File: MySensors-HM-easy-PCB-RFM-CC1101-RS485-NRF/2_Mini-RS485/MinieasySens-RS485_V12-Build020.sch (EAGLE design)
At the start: 38 parts, among them IC1 ATSHA204A, IC2 REG1117, IC4 REG1117, M1 ARDUINO-PRO-MINI-3.3V#NP, X1 1751264, X4 1751264

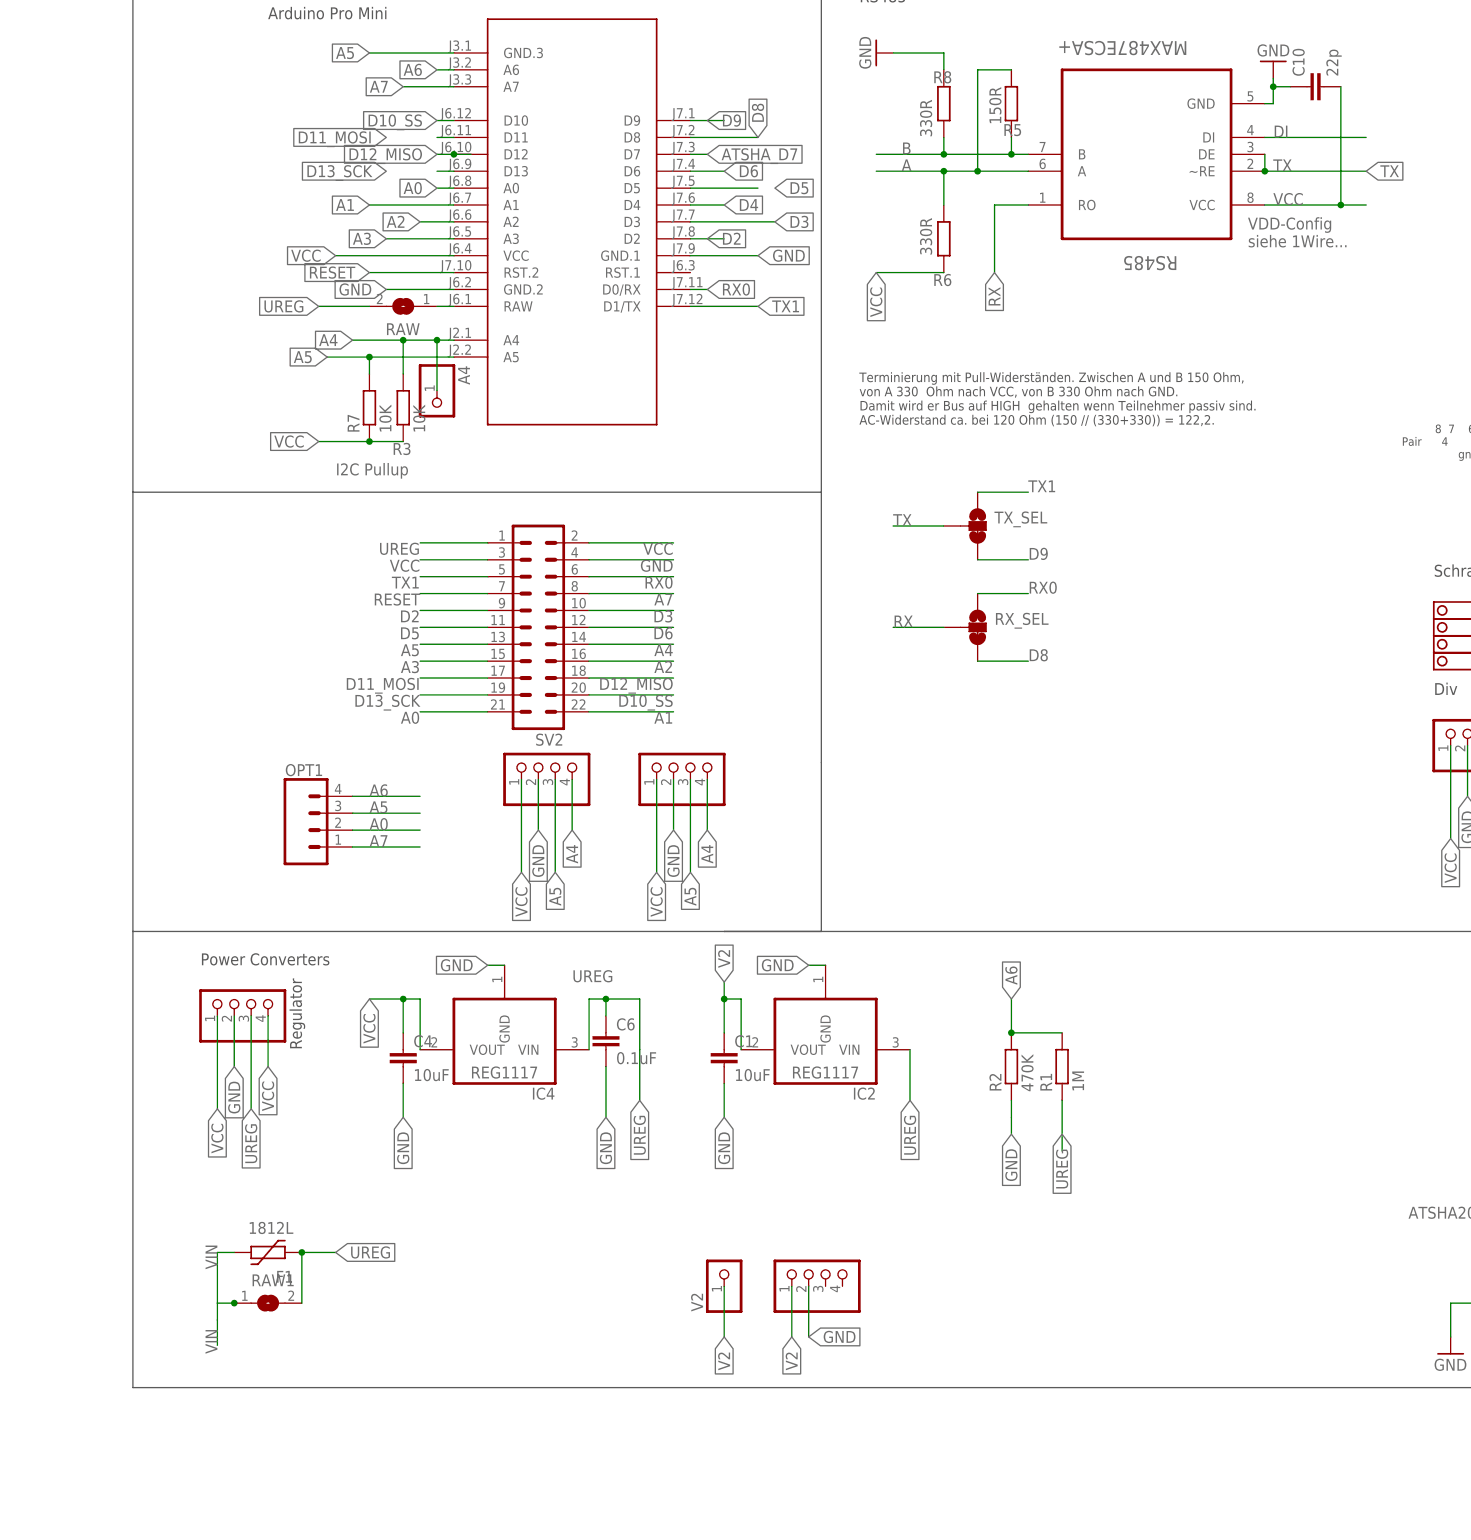
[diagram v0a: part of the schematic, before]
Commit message: BluePill, MiniRS485 Sensor+Gateway
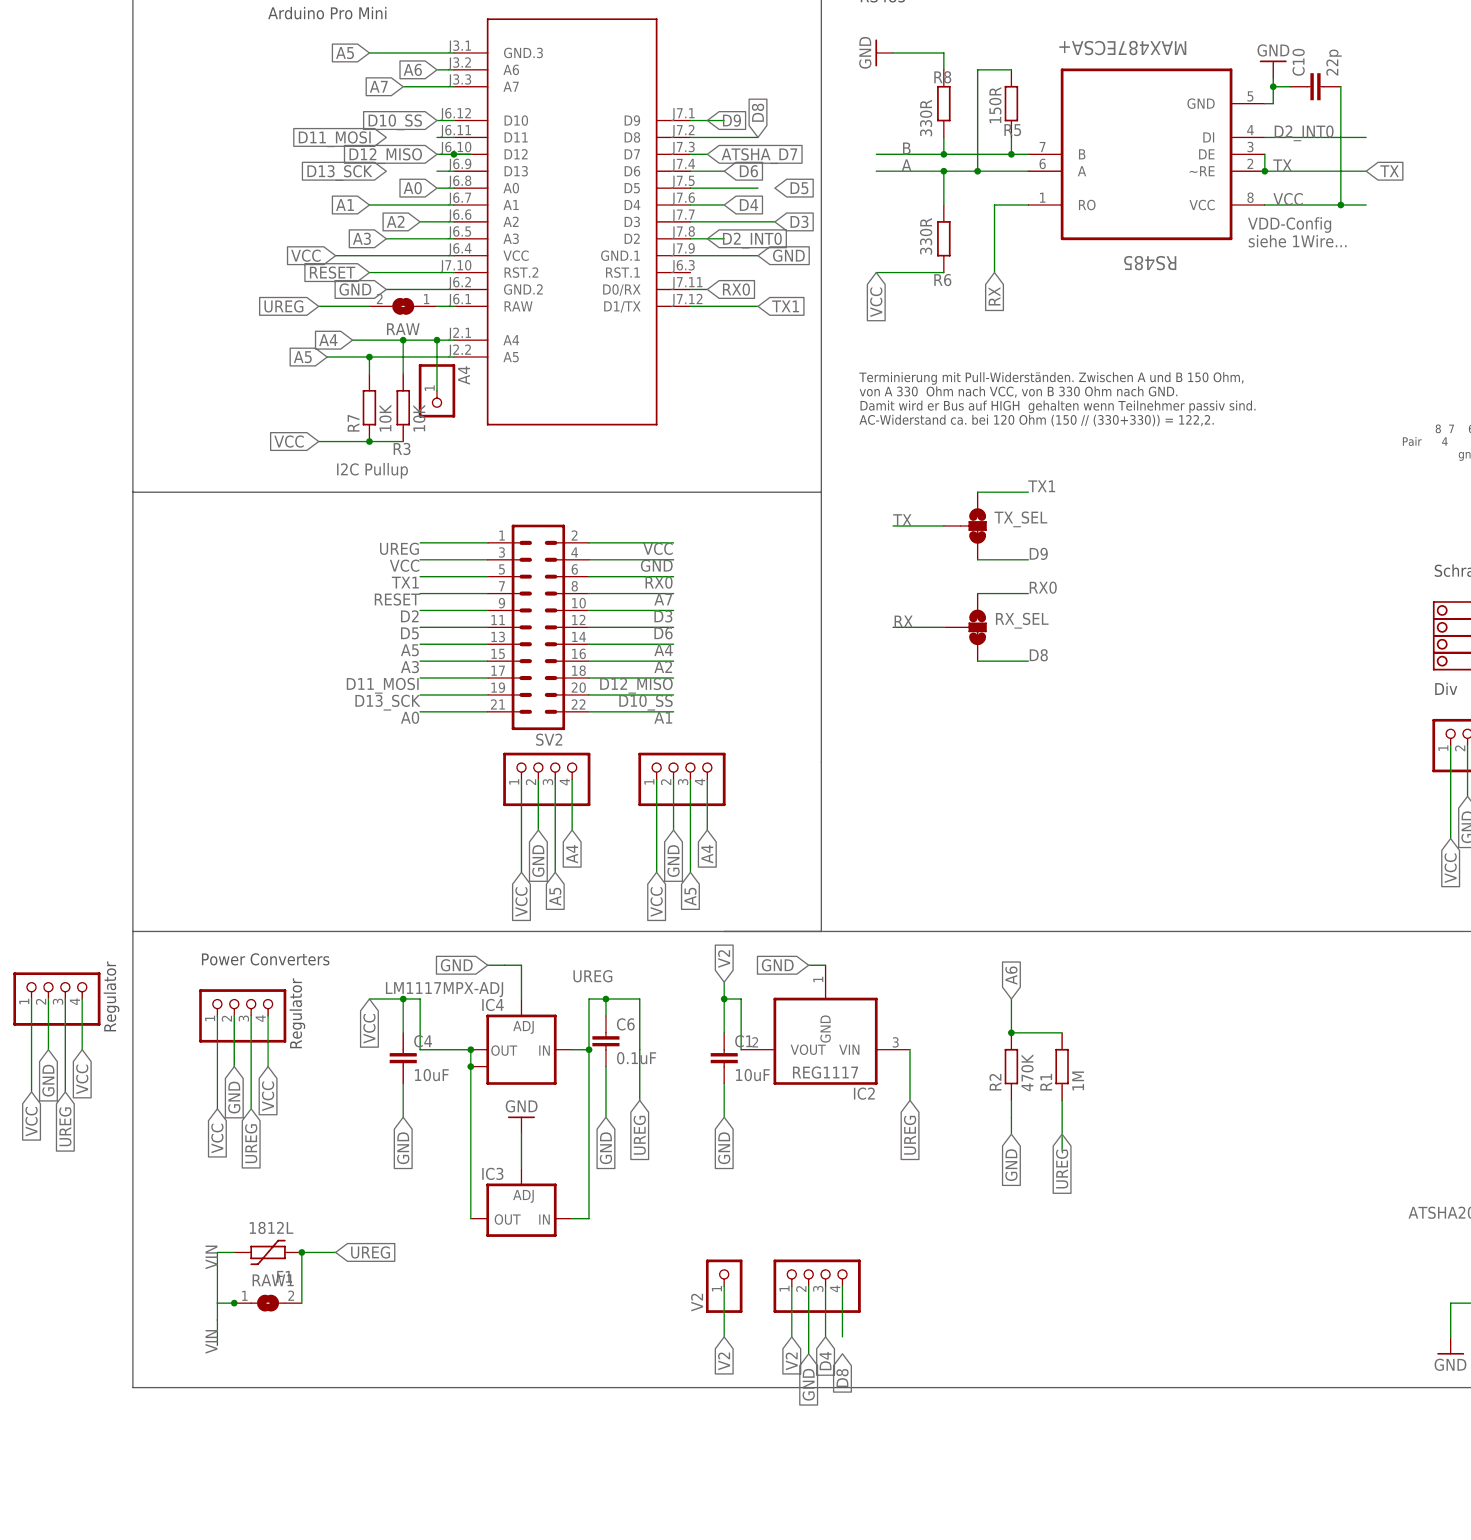
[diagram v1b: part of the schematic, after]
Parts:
- removed OPT1: (no value), SparkFun-Connectors:CONN_04
- added IC3: LD117ADT50TR, v-reg:LD117ADT50TR
- added STEPDWN1: (no value), pinhead-2:PINHD-1X04_2.54-S
- IC4: value REG1117 -> LM1117MPX-ADJ; device burr-brown:REG1117 -> lm1117:LM1117MPX-ADJ
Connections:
- removed net DI: RS485.DI
- new net D2_INT0: M1.D2, RS485.DI
- net A0: no longer OPT1.2
- net A5: no longer OPT1.3
- net A6: no longer OPT1.4
- net A7: no longer OPT1.1
- net D2: no longer M1.D2
- net D4: now also V2-.3
- net D8: now also V2-.4
- net GND: now also IC3.ADJ, IC4.ADJ, STEPDWN1.2; no longer IC4.GND
- net UREG: now also IC3.IN, IC4.IN, STEPDWN1.3; no longer IC4.VIN
- net VCC: now also IC3.OUT, IC4.OUT, IC4.OUT1, STEPDWN1.1, STEPDWN1.4; no longer IC4.VOUT
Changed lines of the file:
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@@
 <?xml version="1.0" encoding="utf-8"?>
 <!DOCTYPE eagle SYSTEM "eagle.dtd">
-<eagle version="7.6.0">
+<eagle version="7.7.0">
 <drawing>
 <settings>
@@
 <part name="C10" library="rcl" deviceset="C-EU" device="C0805" value="22p"/>
 <part name="R8" library="rcl" deviceset="R-EU_" device="R0805" value="330R"/>
-<part name="IC4" library="burr-brown" deviceset="REG1117" device=""/>
-<part name="OPT1" library="SparkFun-Connectors" deviceset="CONN_04" device=""/>
 <part name="STEPDWN" library="pinhead-2" deviceset="PINHD-1X04" device="_2.54-S"/>
 <part name="RAW1" library="jumper" deviceset="SJ" device=""/>
@@
 <part name="JP1" library="pinhead-2" deviceset="PINHD-1X04" device="_2.54-S"/>
 <part name="JP2" library="pinhead-2" deviceset="PINHD-1X04" device="_2.54-S"/>
+<part name="IC3" library="v-reg" deviceset="LD117A?*" device="DT" technology="50TR"/>
+<part name="GND1" library="supply1@1" deviceset="GND" device=""/>
+<part name="IC4" library="lm1117" deviceset="LM1117MPX-ADJ" device=""/>
+<part name="STEPDWN1" library="pinhead-2" deviceset="PINHD-1X04" device="_2.54-S"/>
 </parts>
 <sheets>
@@
 <wire x1="-2.54" y1="73.66" x2="12.065" y2="73.66" width="0.1524" layer="97"/>
 <wire x1="-2.54" y1="73.66" x2="161.925" y2="73.66" width="0.1524" layer="97"/>
+<text x="-93.98" y="58.42" size="1.778" layer="97" rot="R90">Regulator</text>
 </plain>
 <instances>
@@
 <attribute name="VALUE" x="28.702" y="193.04" size="1.778" layer="96" rot="R90"/>
 </instance>
-<instance part="IC4" gate="G$1" x="-35.56" y="55.88" rot="R180"/>
-<instance part="OPT1" gate="G$1" x="-63.5" y="88.9"/>
 <instance part="STEPDWN" gate="A" x="-73.66" y="63.5" smashed="yes" rot="R90">
 <attribute name="VALUE" x="-66.04" y="57.15" size="1.778" layer="96" rot="R90"/>
@@
 <attribute name="VALUE" x="149.86" y="74.93" size="1.778" layer="96" rot="R90"/>
 </instance>
+<instance part="IC3" gate="G$1" x="-33.02" y="30.48" smashed="yes" rot="R180">
+<attribute name="NAME" x="-35.56" y="38.1" size="1.778" layer="95" rot="R180"/>
+</instance>
+<instance part="GND1" gate="1" x="-33.02" y="45.72" rot="R180"/>
+<instance part="IC4" gate="G$1" x="-33.02" y="55.88" rot="R180"/>
+<instance part="STEPDWN1" gate="A" x="-101.6" y="66.04" smashed="yes" rot="R90">
+<attribute name="VALUE" x="-93.98" y="59.69" size="1.778" layer="96" rot="R90"/>
+</instance>
 </instances>
 <busses>
@@
 </segment>
 <segment>
-<pinref part="IC4" gate="G$1" pin="GND"/>
 <wire x1="-35.56" y1="68.58" x2="-38.1" y2="68.58" width="0.1524" layer="91"/>
 <label x="-38.1" y="68.58" size="1.778" layer="95" rot="R180" xref="yes"/>
+<pinref part="IC4" gate="G$1" pin="ADJ"/>
+<wire x1="-35.56" y1="68.58" x2="-33.02" y2="68.58" width="0.1524" layer="91"/>
+<wire x1="-33.02" y1="68.58" x2="-33.02" y2="63.5" width="0.1524" layer="91"/>
 </segment>
 <segment>
@@
 <segment>
 <pinref part="V2-" gate="A" pin="2"/>
-<wire x1="10.16" y1="20.32" x2="10.16" y2="12.7" width="0.1524" layer="91"/>
-<label x="10.16" y="12.7" size="1.778" layer="95" xref="yes"/>
+<wire x1="10.16" y1="20.32" x2="10.16" y2="10.16" width="0.1524" layer="91"/>
+<label x="10.16" y="10.16" size="1.778" layer="95" rot="R270" xref="yes"/>
+</segment>
+<segment>
+<pinref part="IC3" gate="G$1" pin="ADJ"/>
+<pinref part="GND1" gate="1" pin="GND"/>
+<wire x1="-33.02" y1="38.1" x2="-33.02" y2="43.18" width="0.1524" layer="91"/>
+</segment>
+<segment>
+<pinref part="STEPDWN1" gate="A" pin="2"/>
+<wire x1="-104.14" y1="63.5" x2="-104.14" y2="55.88" width="0.1524" layer="91"/>
+<label x="-104.14" y="55.88" size="1.778" layer="95" rot="R270" xref="yes"/>
 </segment>
 </net>
@@
 <junction x="-20.32" y="63.5"/>
 <label x="-25.4" y="66.04" size="1.778" layer="95"/>
-<pinref part="IC4" gate="G$1" pin="VIN"/>
 <wire x1="-22.86" y1="55.88" x2="-22.86" y2="63.5" width="0.1524" layer="91"/>
+<pinref part="IC4" gate="G$1" pin="IN"/>
+<wire x1="-22.86" y1="55.88" x2="-25.4" y2="55.88" width="0.1524" layer="91"/>
+<pinref part="IC3" gate="G$1" pin="IN"/>
+<wire x1="-25.4" y1="30.48" x2="-22.86" y2="30.48" width="0.1524" layer="91"/>
+<wire x1="-22.86" y1="30.48" x2="-22.86" y2="55.88" width="0.1524" layer="91"/>
+<junction x="-22.86" y="55.88"/>
 </segment>
 <segment>
@@
 <wire x1="25.4" y1="55.88" x2="25.4" y2="48.26" width="0.1524" layer="91"/>
 <label x="25.4" y="48.26" size="1.778" layer="95" rot="R270" xref="yes"/>
+</segment>
+<segment>
+<pinref part="STEPDWN1" gate="A" pin="3"/>
+<wire x1="-101.6" y1="63.5" x2="-101.6" y2="49.53" width="0.1524" layer="91"/>
+<label x="-101.6" y="49.53" size="1.778" layer="95" rot="R270" xref="yes"/>
 </segment>
 </net>
@@
 <wire x1="-50.8" y1="63.5" x2="-48.26" y2="63.5" width="0.1524" layer="91"/>
 <junction x="-50.8" y="63.5"/>
-<pinref part="IC4" gate="G$1" pin="VOUT"/>
 <wire x1="-48.26" y1="55.88" x2="-48.26" y2="63.5" width="0.1524" layer="91"/>
+<pinref part="IC4" gate="G$1" pin="OUT"/>
+<wire x1="-40.64" y1="55.88" x2="-48.26" y2="55.88" width="0.1524" layer="91"/>
+<pinref part="IC4" gate="G$1" pin="OUT1"/>
+<wire x1="-40.64" y1="53.34" x2="-40.64" y2="55.88" width="0.1524" layer="91"/>
+<junction x="-40.64" y="55.88"/>
+<pinref part="IC3" gate="G$1" pin="OUT"/>
+<wire x1="-40.64" y1="30.48" x2="-40.64" y2="53.34" width="0.1524" layer="91"/>
+<junction x="-40.64" y="53.34"/>
 </segment>
 <segment>
@@
 <wire x1="-22.86" y1="132.08" x2="-10.16" y2="132.08" width="0.1524" layer="91"/>
 <label x="-10.16" y="132.08" size="1.778" layer="95" rot="R180"/>
+</segment>
+<segment>
+<pinref part="STEPDWN1" gate="A" pin="1"/>
+<wire x1="-106.68" y1="63.5" x2="-106.68" y2="49.53" width="0.1524" layer="91"/>
+<label x="-106.68" y="49.53" size="1.778" layer="95" rot="R270" xref="yes"/>
+</segment>
+<segment>
+<pinref part="STEPDWN1" gate="A" pin="4"/>
+<wire x1="-99.06" y1="63.5" x2="-99.06" y2="55.88" width="0.1524" layer="91"/>
+<label x="-99.06" y="55.88" size="1.778" layer="95" rot="R270" xref="yes"/>
 </segment>
 </net>
@@
 </segment>
 <segment>
-<pinref part="OPT1" gate="G$1" pin="3"/>
-<wire x1="-58.42" y1="91.44" x2="-48.26" y2="91.44" width="0.1524" layer="91"/>
-<label x="-55.88" y="91.44" size="1.778" layer="95"/>
-</segment>
-<segment>
 <pinref part="SV2" gate="1" pin="13"/>
 <wire x1="-48.26" y1="116.84" x2="-38.1" y2="116.84" width="0.1524" layer="91"/>
@@
 <wire x1="-7.62" y1="182.88" x2="-2.54" y2="182.88" width="0.1524" layer="91"/>
 <label x="-2.54" y="182.88" size="1.778" layer="95" xref="yes"/>
+</segment>
+<segment>
+<pinref part="V2-" gate="A" pin="3"/>
+<wire x1="12.7" y1="20.32" x2="12.7" y2="12.7" width="0.1524" layer="91"/>
+<label x="12.7" y="12.7" size="1.778" layer="95" rot="R270" xref="yes"/>
 </segment>
 </net>
@@
 </segment>
 <segment>
-<pinref part="OPT1" gate="G$1" pin="2"/>
-<wire x1="-58.42" y1="88.9" x2="-48.26" y2="88.9" width="0.1524" layer="91"/>
-<label x="-55.88" y="88.9" size="1.778" layer="95"/>
-</segment>
-<segment>
 <pinref part="SV2" gate="1" pin="21"/>
 <wire x1="-38.1" y1="106.68" x2="-48.26" y2="106.68" width="0.1524" layer="91"/>
@@
 <label x="43.18" y="114.3" size="1.778" layer="95"/>
 </segment>
+<segment>
+<pinref part="V2-" gate="A" pin="4"/>
+<wire x1="15.24" y1="20.32" x2="15.24" y2="12.7" width="0.1524" layer="91"/>
+<label x="15.24" y="10.16" size="1.778" layer="95" rot="R270" xref="yes"/>
+</segment>
 </net>
 <net name="D9" class="0">
@@
 <wire x1="-43.18" y1="203.2" x2="-45.72" y2="203.2" width="0.1524" layer="91"/>
 <label x="-45.72" y="203.2" size="1.778" layer="95" rot="R180" xref="yes"/>
-</segment>
-<segment>
-<pinref part="OPT1" gate="G$1" pin="4"/>
-<wire x1="-58.42" y1="93.98" x2="-48.26" y2="93.98" width="0.1524" layer="91"/>
-<label x="-55.88" y="93.98" size="1.778" layer="95"/>
 </segment>
 <segment>
@@
 <wire x1="-43.18" y1="200.66" x2="-50.8" y2="200.66" width="0.1524" layer="91"/>
 <label x="-50.8" y="200.66" size="1.778" layer="95" rot="R180" xref="yes"/>
-</segment>
-<segment>
-<pinref part="OPT1" gate="G$1" pin="1"/>
-<wire x1="-58.42" y1="86.36" x2="-48.26" y2="86.36" width="0.1524" layer="91"/>
-<label x="-55.88" y="86.36" size="1.778" layer="95"/>
 </segment>
 <segment>
@@
 </segment>
 </net>
-<net name="DI" class="0">
-<segment>
-<pinref part="RS485" gate="A" pin="DI"/>
-<wire x1="78.74" y1="193.04" x2="93.98" y2="193.04" width="0.1524" layer="91"/>
-<label x="80.01" y="193.04" size="1.778" layer="95"/>
-</segment>
-</net>
 <net name="VIN" class="1">
 <segment>
@@
 <label x="-48.26" y="121.92" size="1.778" layer="95" rot="R180"/>
 </segment>
-<segment>
-<pinref part="M1" gate="G$1" pin="D2"/>
-<wire x1="-7.62" y1="177.8" x2="-2.54" y2="177.8" width="0.1524" layer="91"/>
-<label x="-5.08" y="177.8" size="1.778" layer="95" xref="yes"/>
-</segment>
 </net>
 <net name="N$2" class="1">
@@
 </segment>
 </net>
+<net name="D2_INT0" class="0">
+<segment>
+<pinref part="M1" gate="G$1" pin="D2"/>
+<wire x1="-7.62" y1="177.8" x2="-2.54" y2="177.8" width="0.1524" layer="91"/>
+<label x="-5.08" y="177.8" size="1.778" layer="95" xref="yes"/>
+</segment>
+<segment>
+<pinref part="RS485" gate="A" pin="DI"/>
+<wire x1="78.74" y1="193.04" x2="93.98" y2="193.04" width="0.1524" layer="91"/>
+<label x="80.01" y="193.04" size="1.778" layer="95"/>
+</segment>
+</net>
